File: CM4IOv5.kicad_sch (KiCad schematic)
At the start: 45 parts, among them J1 Conn_01x02, J2 Bus_M.2_Socket_B, Q1 DMP3013SFV-7, U1 TPS63060DSC (adj), U2 AP64501SP-13

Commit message: Adding 3D modesl
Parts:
- L1: footprint Inductor_SMD:L_Bourns_SRN6045TA -> (none)
- L2: footprint Inductor_SMD:L_Bourns_SRN6045TA -> Inductor_SMD:L_1210_3225Metric

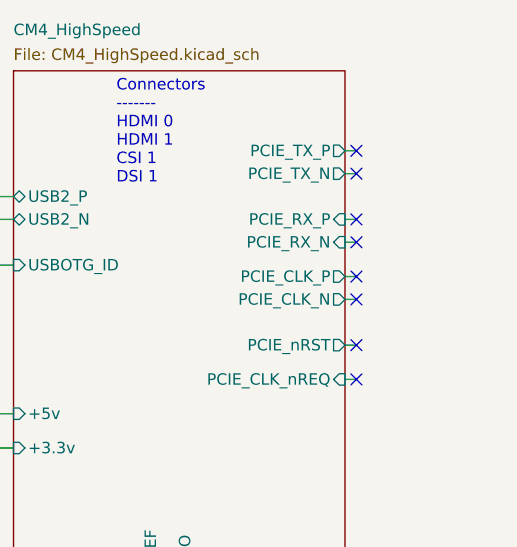
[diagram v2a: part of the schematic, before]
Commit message: Routing High speed signals
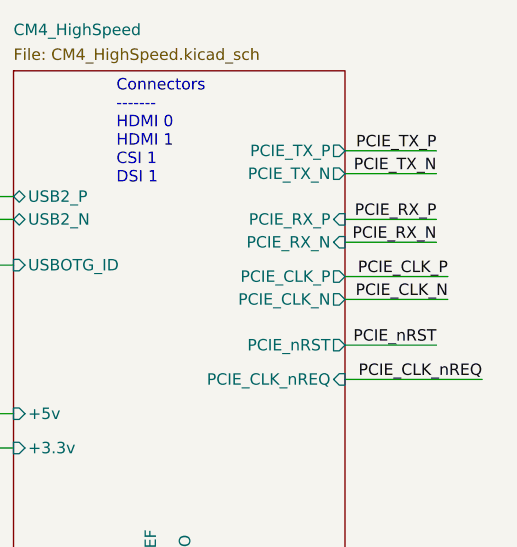
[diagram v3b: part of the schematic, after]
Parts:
- L1: footprint (none) -> Inductor_SMD:L_1210_3225Metric
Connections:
- no-connect marks 36 -> 28

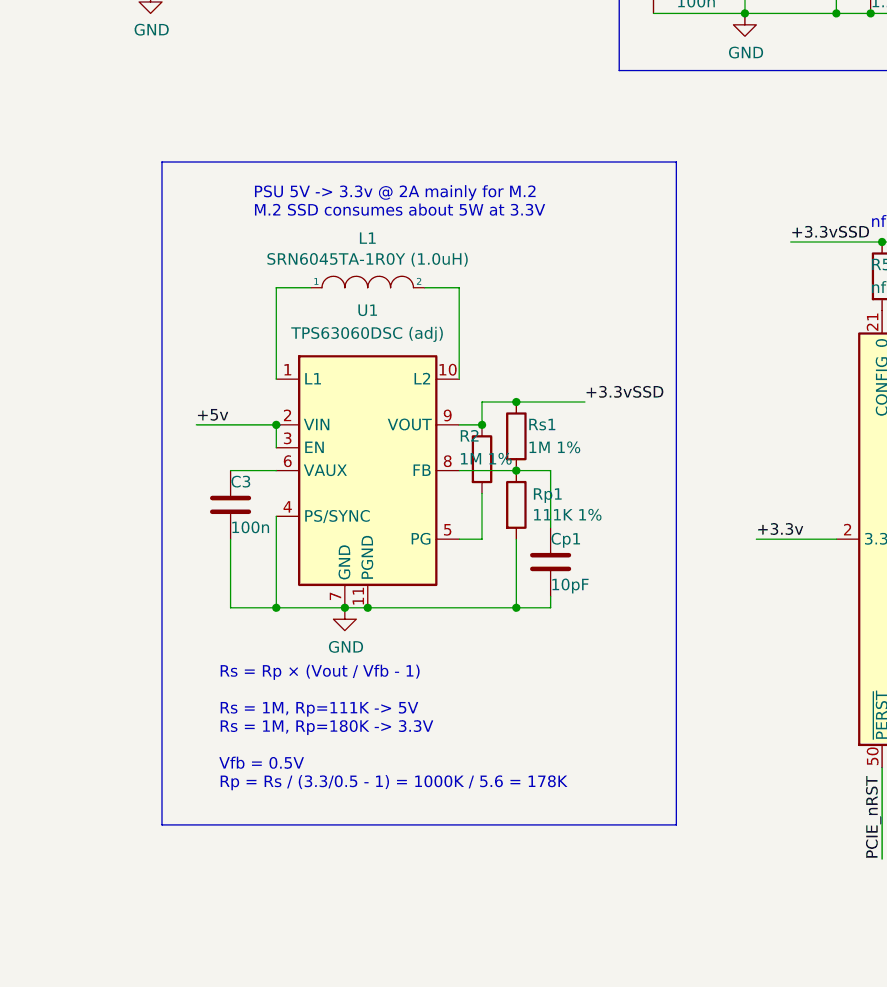
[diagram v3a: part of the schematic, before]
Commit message: Removing U1
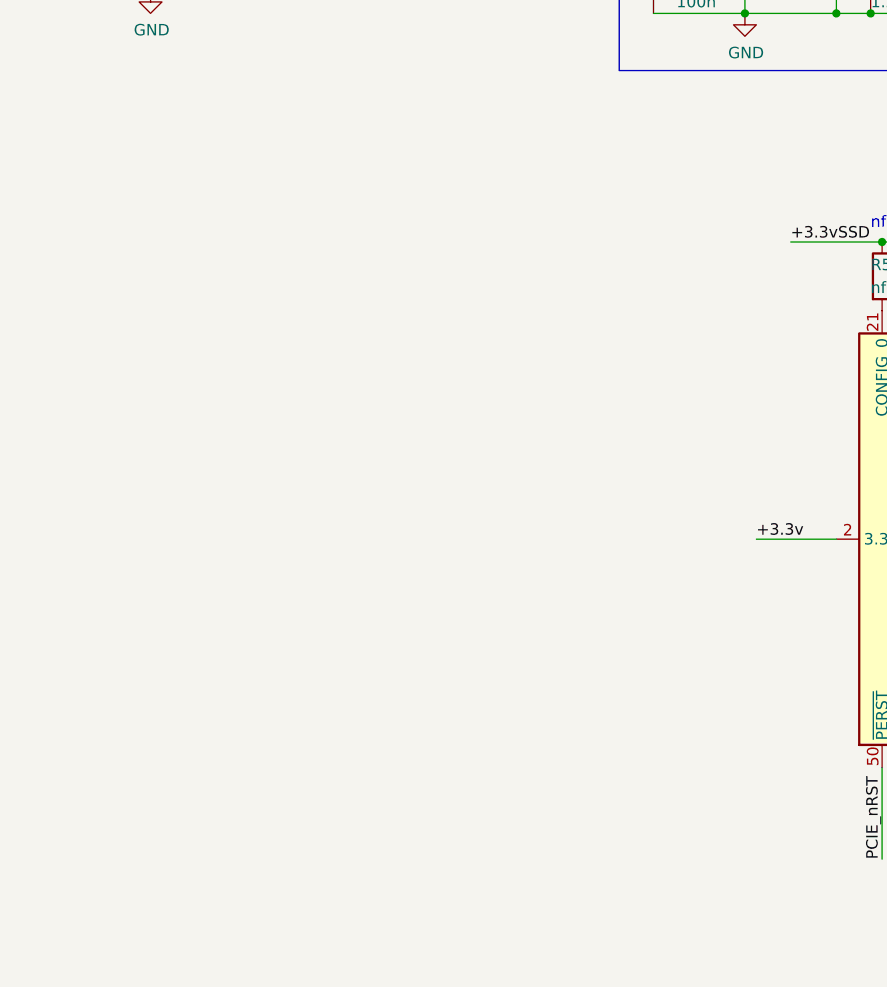
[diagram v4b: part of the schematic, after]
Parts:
- removed C3: 100n, Capacitor_SMD:C_0402_1005Metric, symbol Device:C
- removed Cp1: 10pF, Capacitor_SMD:C_0402_1005Metric, symbol Device:C
- removed L1: SRN6045TA-1R0Y (1.0uH), Inductor_SMD:L_1210_3225Metric, symbol pspice:INDUCTOR
- removed R2, Rs1: 1M 1%, Resistor_SMD:R_0402_1005Metric, symbol Device:R
- removed Rp1: 111K 1%, Resistor_SMD:R_0402_1005Metric, symbol Device:R
- removed U1: TPS63060DSC (adj), Package_SON:Texas_S-PWSON-N10_ThermalVias, symbol Regulator_Switching:TPS63060
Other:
- note removed: "PSU 5V -> 3.3v @ 2A mainly for M.2 M.2 SSD consumes about 5W at 3.3V"
- note removed: "Rs = Rp × (Vout / Vfb - 1) Rs = 1M, Rp=111K -> 5V Rs = 1M, Rp=180K -> 3.3V Vfb = 0.5V Rp = Rs / (3.3/0.5 - 1) = 1000K / 5.6 = 178K"

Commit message: Changing L2
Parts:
- L2: footprint Inductor_SMD:L_1210_3225Metric -> (none)
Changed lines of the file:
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@@
       (effects (font (size 1.27 1.27)))
     )
-    (property "Footprint" "Inductor_SMD:L_1210_3225Metric" (id 2) (at 123.19 31.75 0)
+    (property "Footprint" "" (id 2) (at 123.19 31.75 0)
       (effects (font (size 1.27 1.27)) hide)
     )
@@
     )
     (path "/7252cf63-d7d1-4028-b449-5792fc6d1955"
-      (reference "L2") (unit 1) (value "SRN6045TA-3R3Y  (3.3uH)") (footprint "Inductor_SMD:L_1210_3225Metric")
+      (reference "L2") (unit 1) (value "SRN6045TA-3R3Y  (3.3uH)") (footprint "Inductor_SMD:L_Bourns_SRP7028A_7.3x6.6mm")
     )
     (path "/00000000-0000-0000-0000-00005cff706a/00000000-0000-0000-0000-00005dc6d7d8"

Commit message: Adding GlobalENable, and RpiBoot
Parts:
- L2: footprint (none) -> Inductor_SMD:L_Bourns_SRP7028A_7.3x6.6mm
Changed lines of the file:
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@@
+    (stroke (width 0) (type solid))
+  )
+  (polyline (pts (xy 92.71 20.32) (xy 133.35 20.32))
     (stroke (width 0) (type solid))
   )
@@
     (stroke (width 0) (type solid))
   )
+  (polyline (pts (xy 92.71 20.32) (xy 92.71 69.85))
+    (stroke (width 0) (type solid))
+  )
   (wire (pts (xy 34.29 53.34) (xy 40.64 53.34))
     (stroke (width 0) (type default))
@@
     (stroke (width 0) (type solid))
   )
+  (polyline (pts (xy 133.35 20.32) (xy 133.35 69.85))
+    (stroke (width 0) (type solid))
+  )
   (wire (pts (xy 233.68 83.82) (xy 233.68 99.06))
     (stroke (width 0) (type solid))
@@
     (stroke (width 0) (type default))
   )
-  (polyline (pts (xy 92.71 20.32) (xy 92.71 69.85))
-    (stroke (width 0) (type solid))
-  )
   (wire (pts (xy 54.61 53.34) (xy 59.69 53.34))
     (stroke (width 0) (type solid))
@@
   )
   (wire (pts (xy 96.52 45.72) (xy 96.52 48.26))
-    (stroke (width 0) (type solid))
-  )
-  (polyline (pts (xy 92.71 20.32) (xy 133.35 20.32))
-    (stroke (width 0) (type solid))
-  )
-  (polyline (pts (xy 133.35 20.32) (xy 133.35 69.85))
     (stroke (width 0) (type solid))
   )
@@
       (effects (font (size 1.27 1.27)))
     )
-    (property "Footprint" "" (id 2) (at 123.19 31.75 0)
+    (property "Footprint" "Inductor_SMD:L_Bourns_SRP7028A_7.3x6.6mm" (id 2) (at 123.19 31.75 0)
       (effects (font (size 1.27 1.27)) hide)
     )
@@
       (reference "J11") (unit 1) (value "HDMI_C_1.4") (footprint "CM4IO:EDAC 690-019-298-412")
     )
+    (path "/00000000-0000-0000-0000-00005cff706a/c98cf876-bdd0-4199-98c6-760d4da3c3fa"
+      (reference "J12") (unit 1) (value "nRpiBoot") (footprint "Connector_PinHeader_1.00mm:PinHeader_1x02_P1.00mm_Vertical")
+    )
     (path "/00000000-0000-0000-0000-00005cff706a/00000000-0000-0000-0000-00005e95ca2d"
       (reference "J13") (unit 1) (value "Conn_01x03") (footprint "Connector_PinHeader_2.54mm:PinHeader_1x03_P2.54mm_Vertical")
@@
       (reference "J17") (unit 1) (value "THD-20-R") (footprint "Connector_PinHeader_2.54mm:PinHeader_2x20_P2.54mm_Vertical")
     )
+    (path "/00000000-0000-0000-0000-00005cff706a/da63058d-5bc9-4c2b-8df6-cb51a09aa3b4"
+      (reference "J18") (unit 1) (value "GLOBAL_EN") (footprint "Connector_PinHeader_1.00mm:PinHeader_1x02_P1.00mm_Vertical")
+    )
     (path "/7252cf63-d7d1-4028-b449-5792fc6d1955"

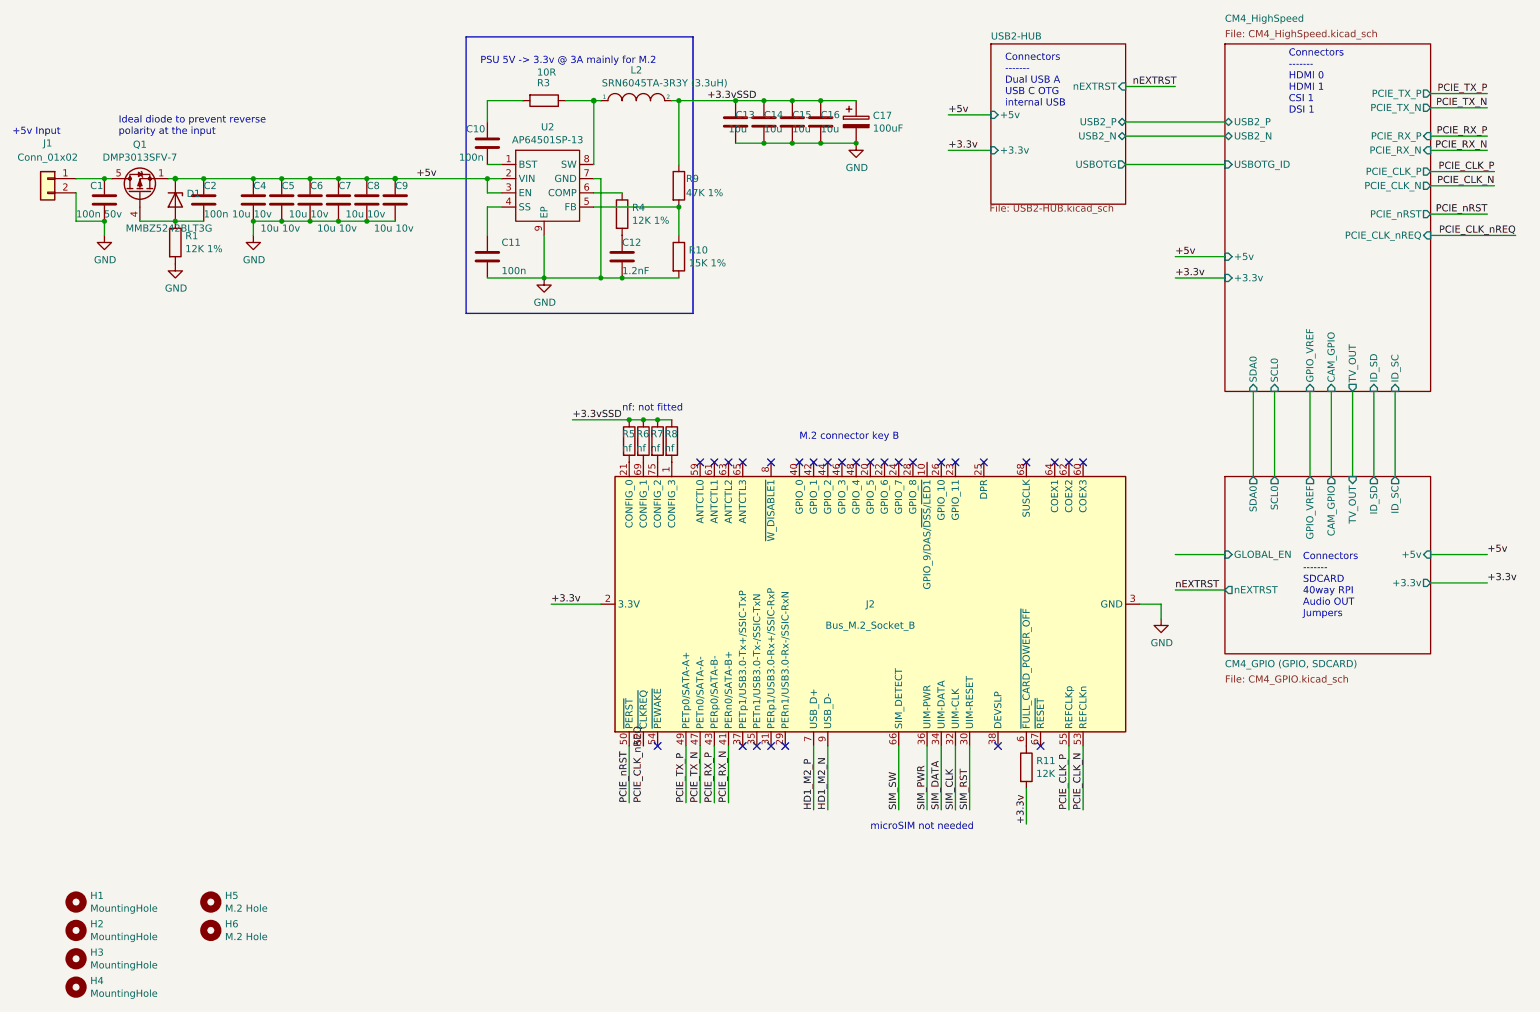
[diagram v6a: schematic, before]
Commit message: Adding audio connector - fixing USB, adding logos
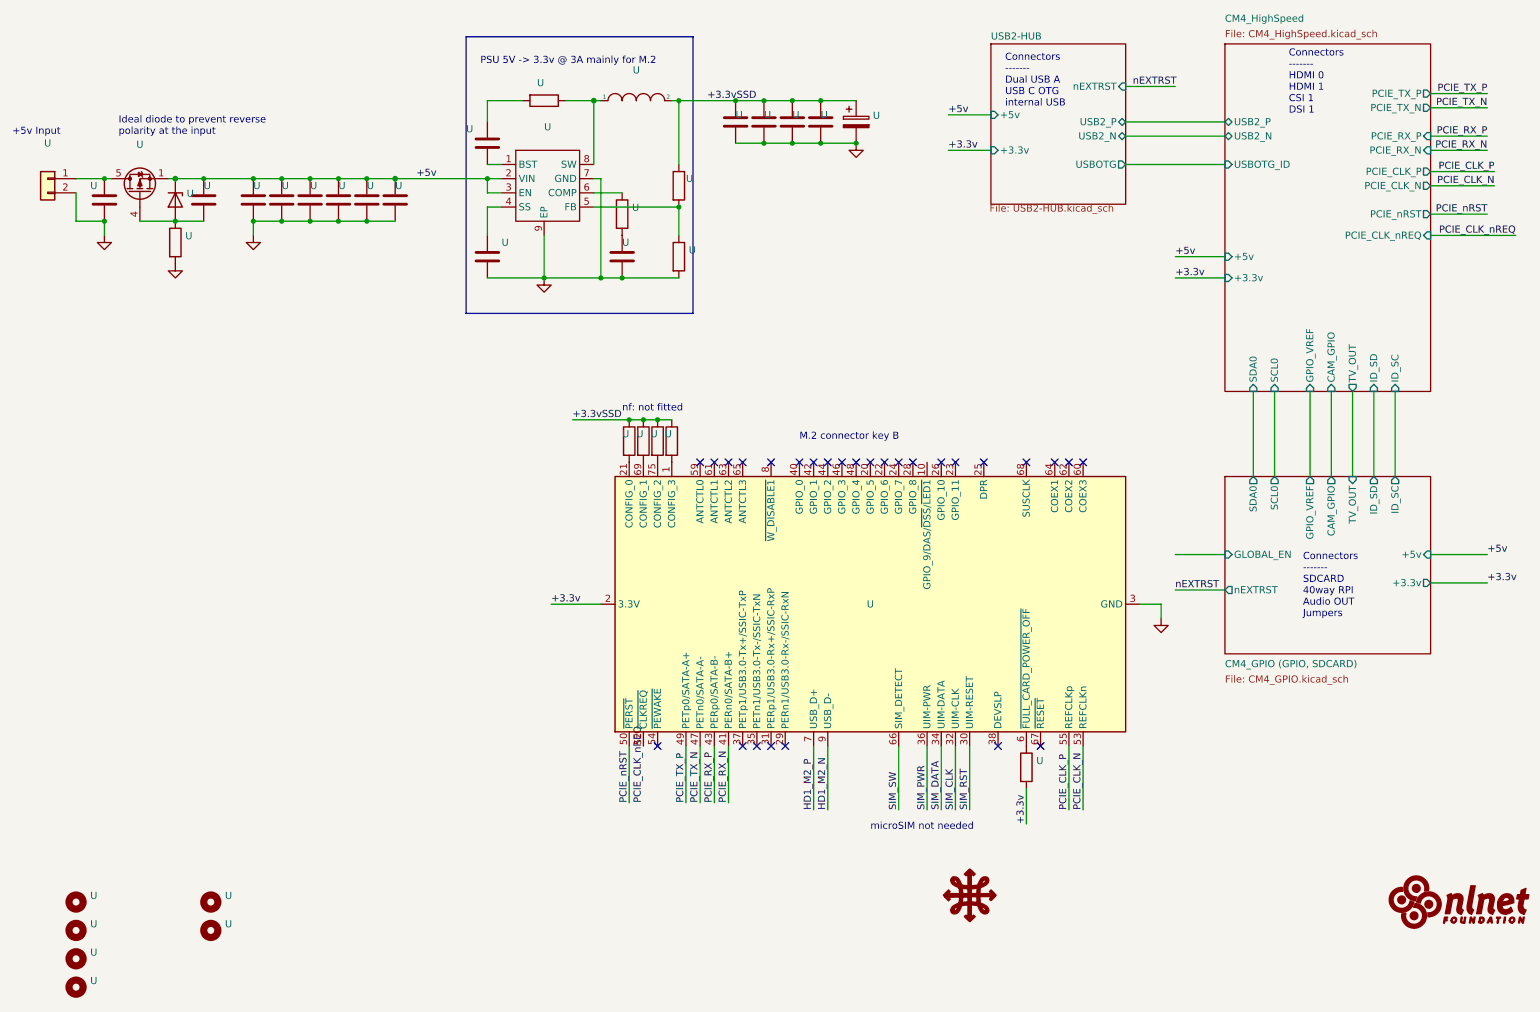
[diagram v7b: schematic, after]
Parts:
- U: renamed from H4; value MountingHole -> (none); footprint MountingHole:MountingHole_2.7mm_M2.5 -> (none)
- U: renamed from H3; value MountingHole -> (none); footprint MountingHole:MountingHole_2.7mm_M2.5 -> (none)
- U: renamed from H2; value MountingHole -> (none); footprint MountingHole:MountingHole_2.7mm_M2.5 -> (none)
- U: renamed from H1; value MountingHole -> (none); footprint MountingHole:MountingHole_2.7mm_M2.5 -> (none)
- U: renamed from C7; value 10u 10v -> (none); footprint Capacitor_SMD:C_0805_2012Metric -> (none)
- U: renamed from R11; value 12K -> (none); footprint Resistor_SMD:R_0402_1005Metric -> (none)
- U: renamed from C13; value 10u -> (none); footprint Capacitor_SMD:C_0805_2012Metric -> (none)
- U: renamed from R8; value nf -> (none); footprint Resistor_SMD:R_0402_1005Metric -> (none)
- U: renamed from C1; value 100n 50v -> (none); footprint Capacitor_SMD:C_0402_1005Metric -> (none)
- U: renamed from C6; value 10u 10v -> (none); footprint Capacitor_SMD:C_0805_2012Metric -> (none)
- U: renamed from R7; value nf -> (none); footprint Resistor_SMD:R_0402_1005Metric -> (none)
- U: renamed from C10; value 100n -> (none); footprint Capacitor_SMD:C_0402_1005Metric -> (none)
- U: renamed from D1; value MMBZ5242BLT3G -> (none); footprint Diode_SMD:D_SOT-23_ANK -> (none)
- U: renamed from C8; value 10u 10v -> (none); footprint Capacitor_SMD:C_0805_2012Metric -> (none)
- U: renamed from C12; value 1.2nF -> (none); footprint Capacitor_SMD:C_0402_1005Metric -> (none)
- U: renamed from R10; value 15K 1% -> (none); footprint Resistor_SMD:R_0402_1005Metric -> (none)
- U: renamed from C11; value 100n -> (none); footprint Capacitor_SMD:C_0402_1005Metric -> (none)
- U: renamed from Q1; value DMP3013SFV-7 -> (none); footprint Package_SON:Diodes_PowerDI3333-8 -> (none)
- U: renamed from R5; value nf -> (none); footprint Resistor_SMD:R_0402_1005Metric -> (none)
- U: renamed from R6; value nf -> (none); footprint Resistor_SMD:R_0402_1005Metric -> (none)
- U: renamed from L2; value SRN6045TA-3R3Y (3.3uH) -> (none); footprint Inductor_SMD:L_Bourns_SRP7028A_7.3x6.6mm -> (none)
- U: renamed from H6; value M.2 Hole -> (none); footprint MountingHole:M.2Hole_3.5mm -> (none)
- U: renamed from C17; value 100uF -> (none); footprint Capacitor_Tantalum_SMD:CP_EIA-7343-31_Kemet-D -> (none)
- U: renamed from C4; value 10u 10v -> (none); footprint Capacitor_SMD:C_0805_2012Metric -> (none)
- U: renamed from C15; value 10u -> (none); footprint Capacitor_SMD:C_0805_2012Metric -> (none)
- U: renamed from J2; value Bus_M.2_Socket_B -> (none); footprint CM4IO:Conn_TE-M.2-0.5-67P-doublesided -> (none)
- U: renamed from U2; value AP64501SP-13 -> (none); footprint Package_SO:SOIC-8-1EP_3.9x4.9mm_P1.27mm_EP2.95x4.9mm_Mask2.71x3.4mm_ThermalVias -> (none)
- U: renamed from C16; value 10u -> (none); footprint Capacitor_SMD:C_0805_2012Metric -> (none)
- U: renamed from C9; value 10u 10v -> (none); footprint Capacitor_SMD:C_0805_2012Metric -> (none)
- U: renamed from C5; value 10u 10v -> (none); footprint Capacitor_SMD:C_0805_2012Metric -> (none)
- U: renamed from R9; value 47K 1% -> (none); footprint Resistor_SMD:R_0402_1005Metric -> (none)
- U: renamed from R3; value 10R -> (none); footprint Resistor_SMD:R_0402_1005Metric -> (none)
- U: renamed from R4; value 12K 1% -> (none); footprint Resistor_SMD:R_0402_1005Metric -> (none)
- U: renamed from J1; value Conn_01x02 -> (none); footprint TerminalBlock:TerminalBlock_bornier-2_P5.08mm -> (none)
- U: renamed from C14; value 10u -> (none); footprint Capacitor_SMD:C_0805_2012Metric -> (none)
- U: renamed from C2; value 100n -> (none); footprint Capacitor_SMD:C_0402_1005Metric -> (none)
- U: renamed from H5; value M.2 Hole -> (none); footprint MountingHole:M.2Hole_3.5mm -> (none)
- U: renamed from R1; value 12K 1% -> (none); footprint Resistor_SMD:R_0402_1005Metric -> (none)
